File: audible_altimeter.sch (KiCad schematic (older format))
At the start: 0 parts

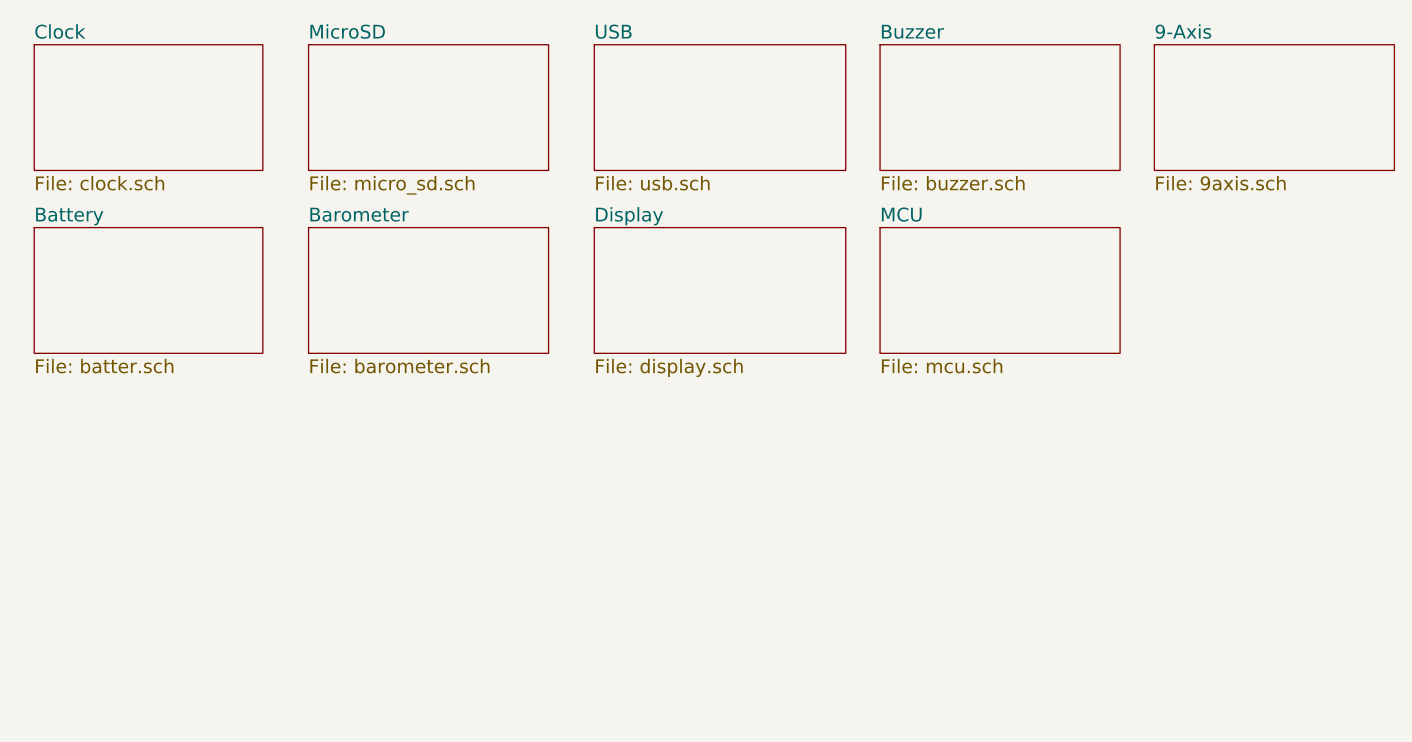
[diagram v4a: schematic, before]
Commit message: Add gps
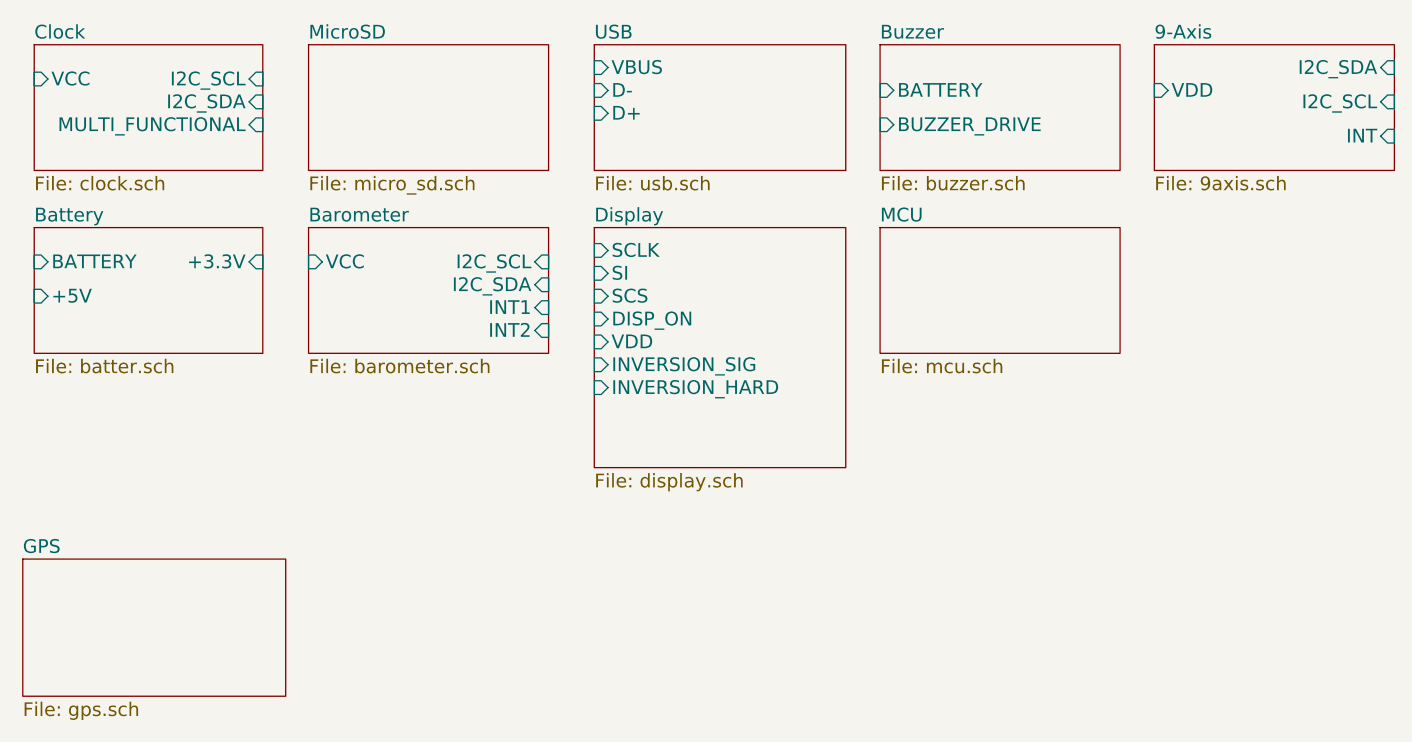
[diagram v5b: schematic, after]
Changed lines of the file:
@@
 $Descr A4 11693 8268
 encoding utf-8
-Sheet 1 10
+Sheet 1 11
 Title ""
 Date ""
@@
 F0 "Clock" 60
 F1 "clock.sch" 60
+F2 "I2C_SCL" I R 3400 3300 60
+F3 "I2C_SDA" I R 3400 3400 60
+F4 "VCC" I L 2400 3300 60
+F5 "MULTI_FUNCTIONAL" I R 3400 3500 60
 $EndSheet
 $Sheet
@@
 F0 "Battery" 60
 F1 "batter.sch" 60
+F2 "BATTERY" I L 2400 4100 60
+F3 "+5V" I L 2400 4250 60
+F4 "+3.3V" I R 3400 4100 60
 $EndSheet
 $Sheet
@@
 F0 "Barometer" 60
 F1 "barometer.sch" 60
+F2 "I2C_SCL" I R 4650 4100 60
+F3 "I2C_SDA" I R 4650 4200 60
+F4 "INT1" I R 4650 4300 60
+F5 "INT2" I R 4650 4400 60
+F6 "VCC" I L 3600 4100 60
 $EndSheet
 $Sheet
@@
 F0 "USB" 60
 F1 "usb.sch" 60
+F2 "VBUS" I L 4850 3250 60
+F3 "D-" I L 4850 3350 60
+F4 "D+" I L 4850 3450 60
 $EndSheet
 $Sheet
-S 4850 3950 1100 550
+S 4850 3950 1100 1050
 U 54463818
 F0 "Display" 60
 F1 "display.sch" 60
+F2 "SCLK" I L 4850 4050 60
+F3 "SI" I L 4850 4150 60
+F4 "SCS" I L 4850 4250 60
+F5 "DISP_ON" I L 4850 4350 60
+F6 "VDD" I L 4850 4450 60
+F7 "INVERSION_SIG" I L 4850 4550 60
+F8 "INVERSION_HARD" I L 4850 4650 60
 $EndSheet
 $Sheet
@@
 F0 "Buzzer" 60
 F1 "buzzer.sch" 60
+F2 "BATTERY" I L 6100 3350 60
+F3 "BUZZER_DRIVE" I L 6100 3500 60
 $EndSheet
 $Sheet
@@
 F0 "9-Axis" 60
 F1 "9axis.sch" 60
+F2 "VDD" I L 7300 3350 60
+F3 "I2C_SDA" I R 8350 3250 60
+F4 "I2C_SCL" I R 8350 3400 60
+F5 "INT" I R 8350 3550 60
+$EndSheet
+$Sheet
+S 2350 5400 1150 600
+U 5461699E
+F0 "GPS" 60
+F1 "gps.sch" 60
 $EndSheet
 $EndSCHEMATC

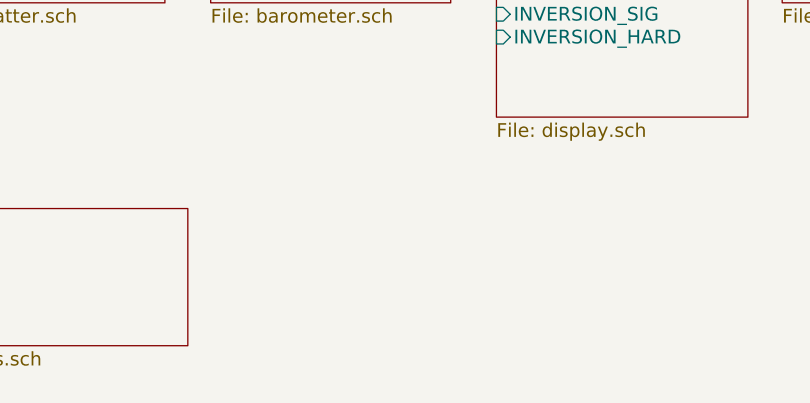
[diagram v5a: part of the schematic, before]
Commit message: Add humidity sensor
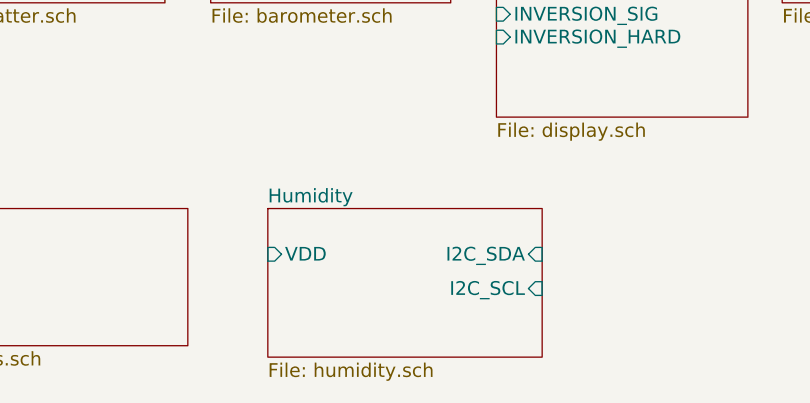
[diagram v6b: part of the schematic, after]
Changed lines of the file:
@@
 $Descr A4 11693 8268
 encoding utf-8
-Sheet 1 11
+Sheet 1 12
 Title ""
 Date ""
@@
 F1 "gps.sch" 60
 $EndSheet
+$Sheet
+S 3850 5400 1200 650
+U 5461BBD1
+F0 "Humidity" 60
+F1 "humidity.sch" 60
+F2 "I2C_SDA" I R 5050 5600 60
+F3 "VDD" I L 3850 5600 60
+F4 "I2C_SCL" I R 5050 5750 60
+$EndSheet
 $EndSCHEMATC

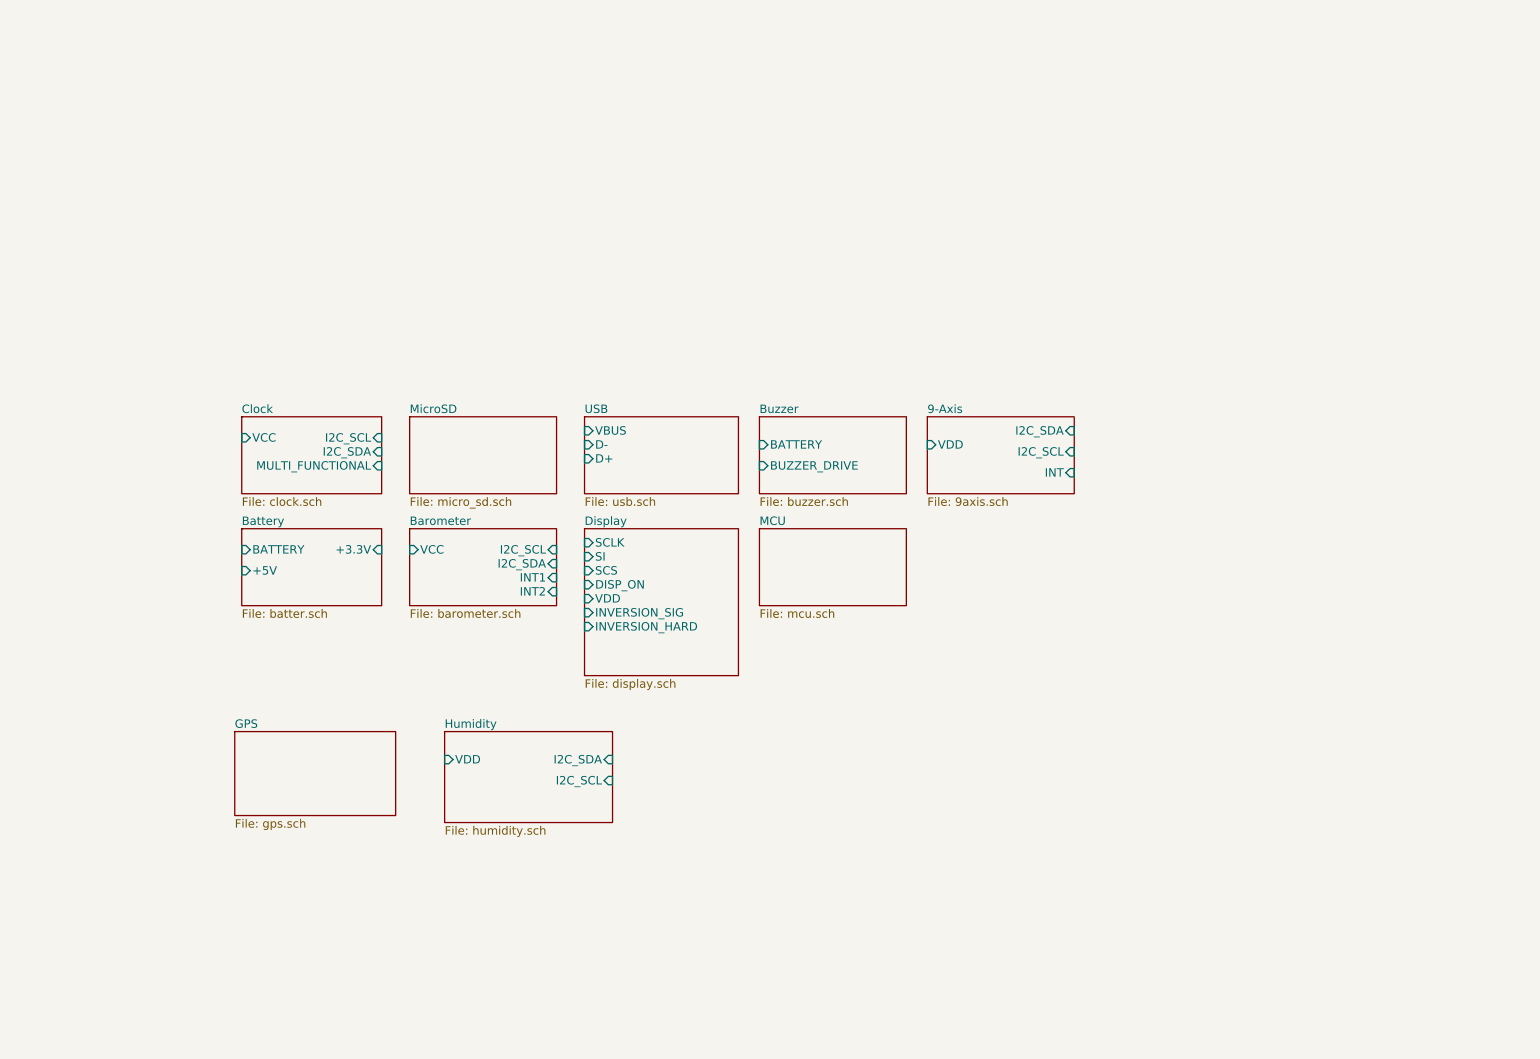
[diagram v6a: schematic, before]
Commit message: More connections
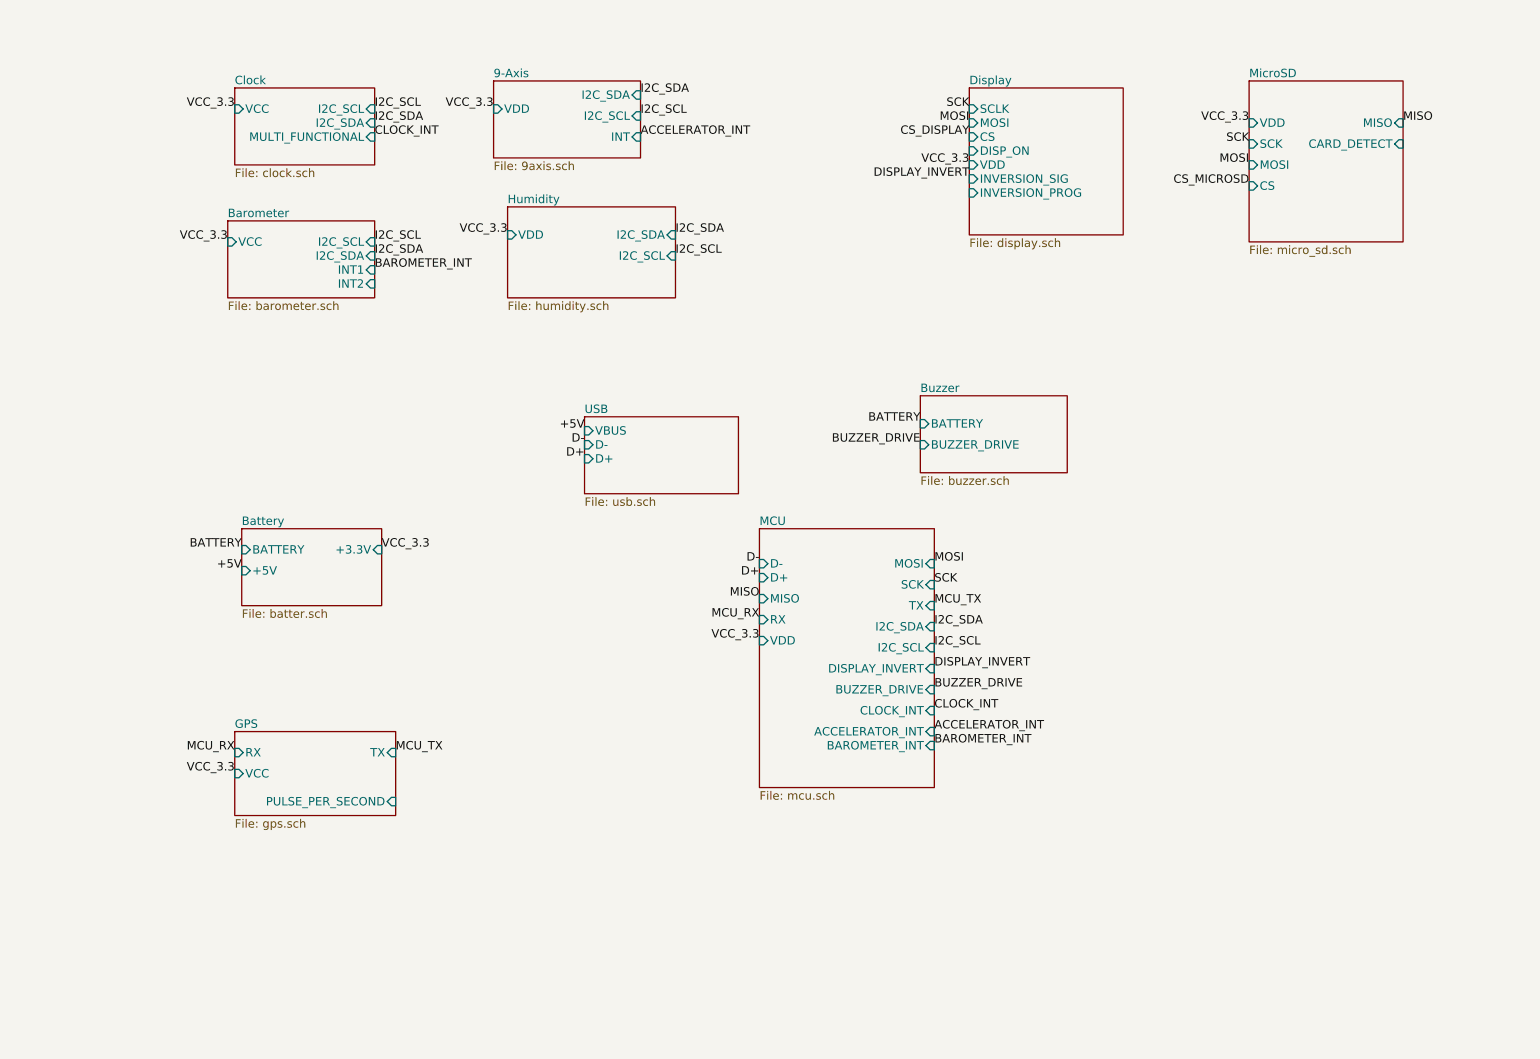
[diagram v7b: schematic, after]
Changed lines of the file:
@@
 $EndDescr
 $Sheet
-S 2400 3150 1000 550
+S 2350 800  1000 550
 U 5446056F
 F0 "Clock" 60
 F1 "clock.sch" 60
-F2 "I2C_SCL" I R 3400 3300 60
-F3 "I2C_SDA" I R 3400 3400 60
-F4 "VCC" I L 2400 3300 60
-F5 "MULTI_FUNCTIONAL" I R 3400 3500 60
+F2 "I2C_SCL" I R 3350 950 60
+F3 "I2C_SDA" I R 3350 1050 60
+F4 "VCC" I L 2350 950 60
+F5 "MULTI_FUNCTIONAL" I R 3350 1150 60
 $EndSheet
 $Sheet
@@
 $EndSheet
 $Sheet
-S 3600 3150 1050 550
+S 9600 750  1100 1150
 U 54462395
 F0 "MicroSD" 60
 F1 "micro_sd.sch" 60
-$EndSheet
-$Sheet
-S 3600 3950 1050 550
+F2 "VDD" I L 9600 1050 60
+F3 "SCK" I L 9600 1200 60
+F4 "MISO" I R 10700 1050 60
+F5 "MOSI" I L 9600 1350 60
+F6 "CS" I L 9600 1500 60
+F7 "CARD_DETECT" I R 10700 1200 60
+$EndSheet
+$Sheet
+S 2300 1750 1050 550
 U 54462AE3
 F0 "Barometer" 60
 F1 "barometer.sch" 60
-F2 "I2C_SCL" I R 4650 4100 60
-F3 "I2C_SDA" I R 4650 4200 60
-F4 "INT1" I R 4650 4300 60
-F5 "INT2" I R 4650 4400 60
-F6 "VCC" I L 3600 4100 60
+F2 "I2C_SCL" I R 3350 1900 60
+F3 "I2C_SDA" I R 3350 2000 60
+F4 "INT1" I R 3350 2100 60
+F5 "INT2" I R 3350 2200 60
+F6 "VCC" I L 2300 1900 60
 $EndSheet
 $Sheet
@@
 $EndSheet
 $Sheet
-S 4850 3950 1100 1050
+S 7600 800  1100 1050
 U 54463818
 F0 "Display" 60
 F1 "display.sch" 60
-F2 "SCLK" I L 4850 4050 60
-F3 "SI" I L 4850 4150 60
-F4 "SCS" I L 4850 4250 60
-F5 "DISP_ON" I L 4850 4350 60
-F6 "VDD" I L 4850 4450 60
-F7 "INVERSION_SIG" I L 4850 4550 60
-F8 "INVERSION_HARD" I L 4850 4650 60
-$EndSheet
-$Sheet
-S 6100 3150 1050 550
+F2 "SCLK" I L 7600 950 60
+F3 "MOSI" I L 7600 1050 60
+F4 "CS" I L 7600 1150 60
+F5 "DISP_ON" I L 7600 1250 60
+F6 "VDD" I L 7600 1350 60
+F7 "INVERSION_SIG" I L 7600 1450 60
+F8 "INVERSION_PROG" I L 7600 1550 60
+$EndSheet
+$Sheet
+S 7250 3000 1050 550
 U 54464246
 F0 "Buzzer" 60
 F1 "buzzer.sch" 60
-F2 "BATTERY" I L 6100 3350 60
-F3 "BUZZER_DRIVE" I L 6100 3500 60
-$EndSheet
-$Sheet
-S 6100 3950 1050 550
+F2 "BATTERY" I L 7250 3200 60
+F3 "BUZZER_DRIVE" I L 7250 3350 60
+$EndSheet
+$Sheet
+S 6100 3950 1250 1850
 U 54464A80
 F0 "MCU" 60
 F1 "mcu.sch" 60
-$EndSheet
-$Sheet
-S 7300 3150 1050 550
+F2 "D-" I L 6100 4200 60
+F3 "D+" I L 6100 4300 60
+F4 "MOSI" I R 7350 4200 60
+F5 "MISO" I L 6100 4450 60
+F6 "SCK" I R 7350 4350 60
+F7 "RX" I L 6100 4600 60
+F8 "TX" I R 7350 4500 60
+F9 "I2C_SDA" I R 7350 4650 60
+F10 "I2C_SCL" I R 7350 4800 60
+F11 "VDD" I L 6100 4750 60
+F12 "DISPLAY_INVERT" I R 7350 4950 60
+F13 "BUZZER_DRIVE" I R 7350 5100 60
+F14 "CLOCK_INT" I R 7350 5250 60
+F15 "ACCELERATOR_INT" I R 7350 5400 60
+F16 "BAROMETER_INT" I R 7350 5500 60
+$EndSheet
+$Sheet
+S 4200 750  1050 550
 U 544655FD
 F0 "9-Axis" 60
 F1 "9axis.sch" 60
-F2 "VDD" I L 7300 3350 60
-F3 "I2C_SDA" I R 8350 3250 60
-F4 "I2C_SCL" I R 8350 3400 60
-F5 "INT" I R 8350 3550 60
+F2 "VDD" I L 4200 950 60
+F3 "I2C_SDA" I R 5250 850 60
+F4 "I2C_SCL" I R 5250 1000 60
+F5 "INT" I R 5250 1150 60
 $EndSheet
 $Sheet
@@
 F0 "GPS" 60
 F1 "gps.sch" 60
-$EndSheet
-$Sheet
-S 3850 5400 1200 650
+F2 "TX" I R 3500 5550 60
+F3 "RX" I L 2350 5550 60
+F4 "VCC" I L 2350 5700 60
+F5 "PULSE_PER_SECOND" I R 3500 5900 60
+$EndSheet
+$Sheet
+S 4300 1650 1200 650
 U 5461BBD1
 F0 "Humidity" 60
 F1 "humidity.sch" 60
-F2 "I2C_SDA" I R 5050 5600 60
-F3 "VDD" I L 3850 5600 60
-F4 "I2C_SCL" I R 5050 5750 60
-$EndSheet
+F2 "I2C_SDA" I R 5500 1850 60
+F3 "VDD" I L 4300 1850 60
+F4 "I2C_SCL" I R 5500 2000 60
+$EndSheet
+Text Label 3350 950  0    60   ~ 0
+I2C_SCL
+Text Label 3350 1900 0    60   ~ 0
+I2C_SCL
+Text Label 5250 1000 0    60   ~ 0
+I2C_SCL
+Text Label 5500 2000 0    60   ~ 0
+I2C_SCL
+Text Label 5500 1850 0    60   ~ 0
+I2C_SDA
+Text Label 5250 850  0    60   ~ 0
+I2C_SDA
+Text Label 3350 1050 0    60   ~ 0
+I2C_SDA
+Text Label 3350 2000 0    60   ~ 0
+I2C_SDA
+Text Label 3400 4100 0    60   ~ 0
+VCC_3.3
+Text Label 2300 1900 2    60   ~ 0
+VCC_3.3
+Text Label 2350 950  2    60   ~ 0
+VCC_3.3
+Text Label 4200 950  2    60   ~ 0
+VCC_3.3
+Text Label 4300 1850 2    60   ~ 0
+VCC_3.3
+Text Label 7600 1350 2    60   ~ 0
+VCC_3.3
+Text Label 7600 950  2    60   ~ 0
+SCK
+Text Label 9600 1050 2    60   ~ 0
+VCC_3.3
+Text Label 9600 1200 2    60   ~ 0
+SCK
+Text Label 9600 1350 2    60   ~ 0
+MOSI
+Text Label 9600 1500 2    60   ~ 0
+CS_MICROSD
+Text Label 7600 1150 2    60   ~ 0
+CS_DISPLAY
+Text Label 7600 1050 2    60   ~ 0
+MOSI
+Text Label 10700 1050 0    60   ~ 0
+MISO
+Text Label 7350 4500 0    60   ~ 0
+MCU_TX
+Text Label 6100 4600 2    60   ~ 0
+MCU_RX
+Text Label 2350 5550 2    60   ~ 0
+MCU_RX
+Text Label 3500 5550 0    60   ~ 0
+MCU_TX
+Text Label 2350 5700 2    60   ~ 0
+VCC_3.3
+Text Label 7350 4200 0    60   ~ 0
+MOSI
+Text Label 7350 4350 0    60   ~ 0
+SCK
+Text Label 6100 4450 2    60   ~ 0
+MISO
+Text Label 6100 4200 2    60   ~ 0
+D-
+Text Label 6100 4300 2    60   ~ 0
+D+
+Text Label 4850 3350 2    60   ~ 0
+D-
+Text Label 4850 3450 2    60   ~ 0
+D+
+Text Label 4850 3250 2    60   ~ 0
++5V
+Text Label 2400 4250 2    60   ~ 0
++5V
+Text Label 2400 4100 2    60   ~ 0
+BATTERY
+Text Label 7250 3200 2    60   ~ 0
+BATTERY
+Text Label 6100 4750 2    60   ~ 0
+VCC_3.3
+Text Label 7350 4800 0    60   ~ 0
+I2C_SCL
+Text Label 7350 4650 0    60   ~ 0
+I2C_SDA
+Text Label 7250 3350 2    60   ~ 0
+BUZZER_DRIVE
+Text Label 7350 5100 0    60   ~ 0
+BUZZER_DRIVE
+Text Label 7350 4950 0    60   ~ 0
+DISPLAY_INVERT
+Text Label 7600 1450 2    60   ~ 0
+DISPLAY_INVERT
+Text Label 7350 5250 0    60   ~ 0
+CLOCK_INT
+Text Label 3350 1150 0    60   ~ 0
+CLOCK_INT
+Text Label 3350 2100 0    60   ~ 0
+BAROMETER_INT
+Text Label 7350 5500 0    60   ~ 0
+BAROMETER_INT
+Text Label 7350 5400 0    60   ~ 0
+ACCELERATOR_INT
+Text Label 5250 1150 0    60   ~ 0
+ACCELERATOR_INT
 $EndSCHEMATC
